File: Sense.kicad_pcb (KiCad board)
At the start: 4 copper layers, 15.2 x 10.2 mm, 10 parts, among them J1 Callistated 1, J2 Callistated 2, U1 SPL07, U2 MMC5603NJ, U3 LSM6DSO32

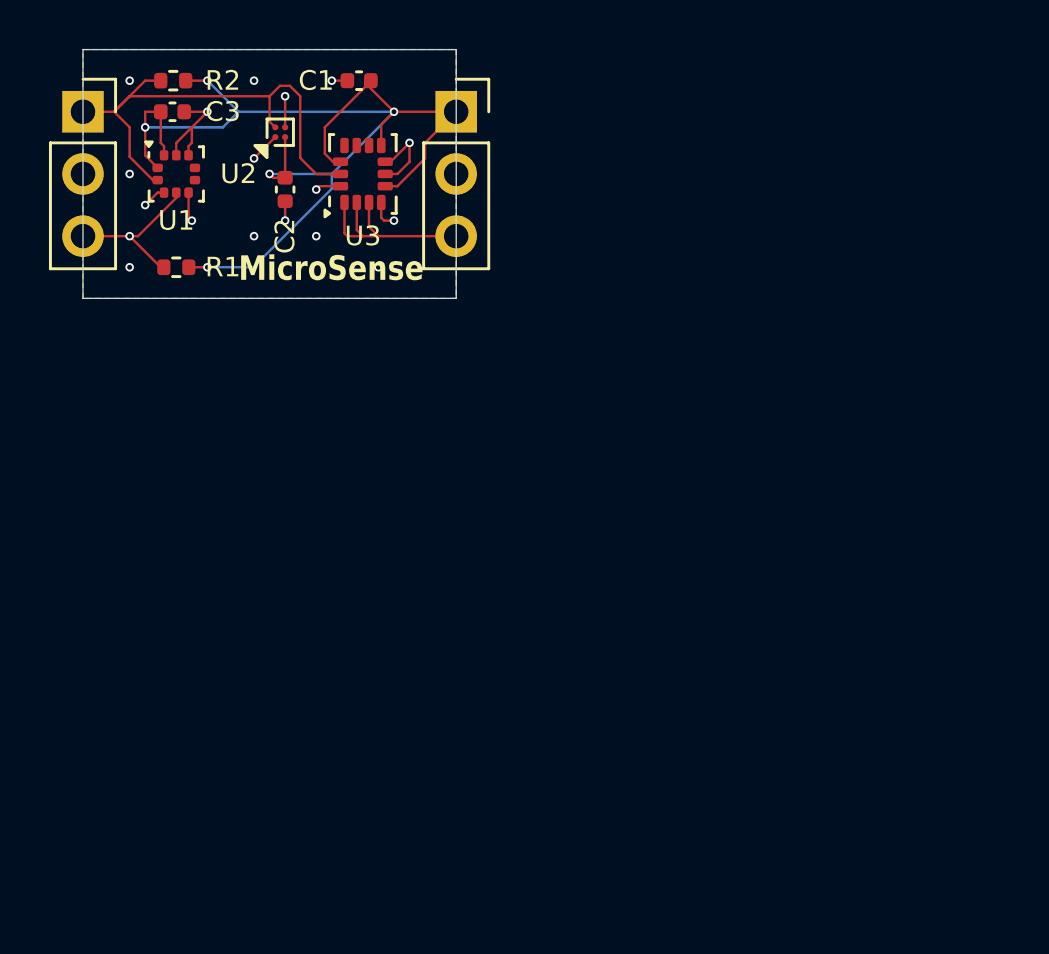
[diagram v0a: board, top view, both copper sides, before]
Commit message: Abandoned castellated pads, updated with LCSC parts
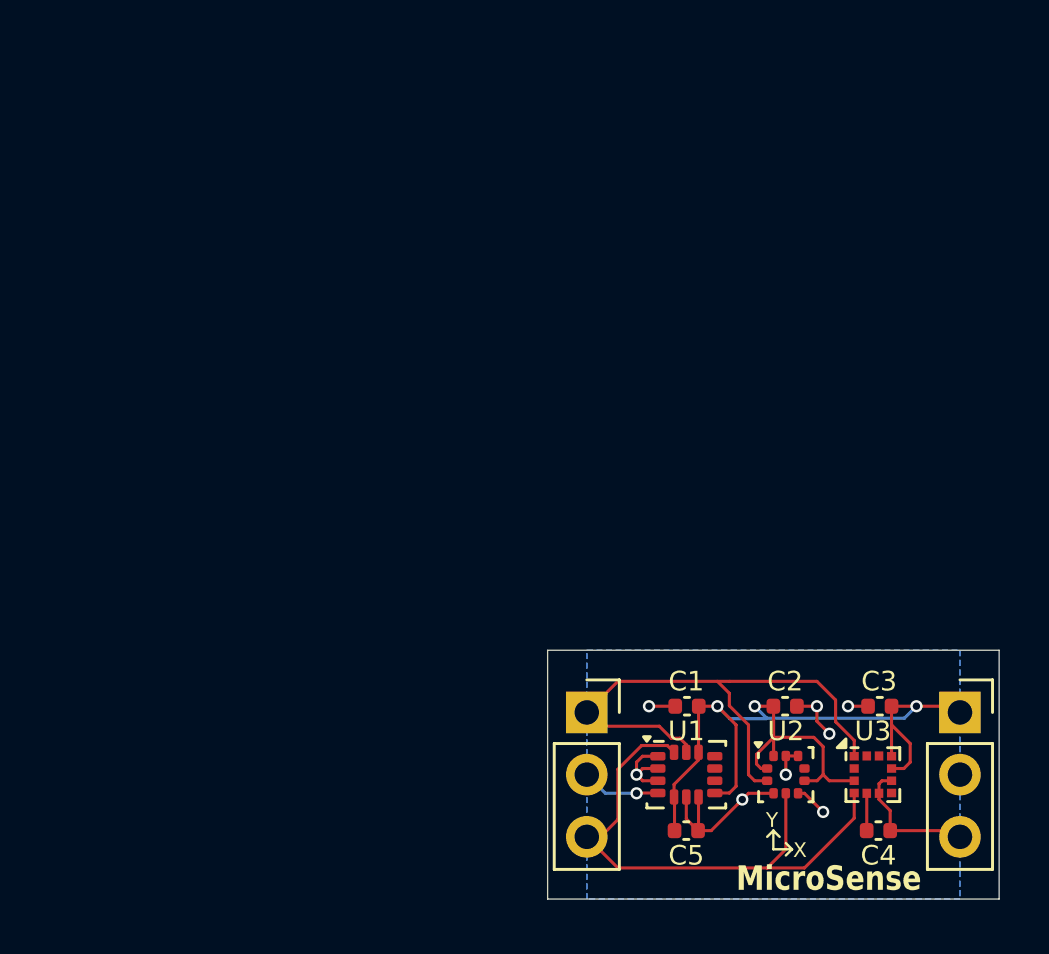
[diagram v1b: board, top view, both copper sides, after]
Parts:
- removed R1, R2: 4K7, Resistor_SMD:R_0402_1005Metric
- removed the U1 at (118.1, 77.5)
- added C4: 220n, Capacitor_SMD:C_0402_1005Metric, F.Cu at (146.8, 104.3)
- added C5: 10u, Capacitor_SMD:C_0402_1005Metric, F.Cu at (138.9, 104.3)
- added U3: LIS2MDL, Package_LGA:LGA-12_2x2mm_P0.5mm, F.Cu at (146.6, 102.0)
- C2: value 2.2u -> 100n
- U2: value MMC5603NJ -> LPS22HB; footprint Package_BGA:WLP-4_0.86x0.86mm_P0.4mm -> Package_LGA:ST_HLGA-10_2x2mm_P0.5mm_LayoutBorder3x2y
- moved C3 37.7 mm to (146.8, 99.2), turned to 180 degrees
- moved U2 33.4 mm to (143.0, 102.0), turned to 0 degrees
- moved J2 32.0 mm to (150.1, 99.5)
- moved J1 32.0 mm to (134.9, 99.5)
- moved C2 29.4 mm to (143.0, 99.2), turned to 0 degrees
- moved C1 28.8 mm to (139.0, 99.2)
- moved U1 27.9 mm to (138.9, 102.0), turned to 0 degrees
- renumbered U3 to U1
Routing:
- net /IMU_INT_1: track 16.1 -> 2.99 mm
- net +3V3: track 48.3 -> 37.4 mm, vias 5 -> 3
- net /SCL: track 20.8 -> 23.3 mm
- net Net-(U3-C1): track 0.00 -> 1.53 mm
- net GND: track 20.9 -> 22.2 mm, vias 14 -> 8
- net /SDA: track 22.6 -> 22.3 mm, vias 3 -> 0
- removed copper zone on In1.Cu, net GND
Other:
- board size 15.2 x 10.2 mm -> 18.4 x 10.2 mm
- copper layers 4 -> 2
- board text added: "X"
- board text added: "Y"

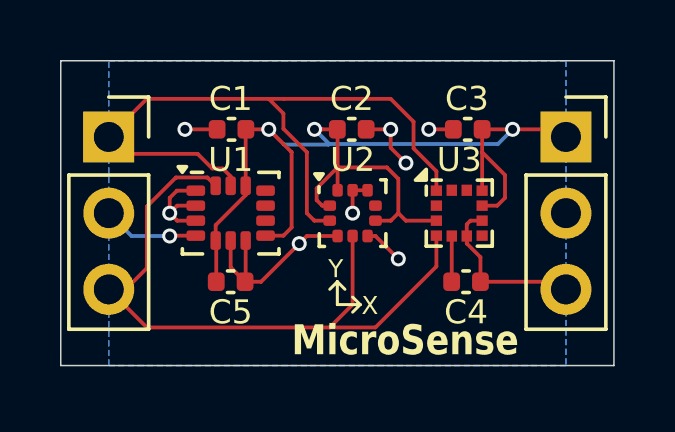
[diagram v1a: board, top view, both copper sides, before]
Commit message: Version C.0
Added high g accelerometer option
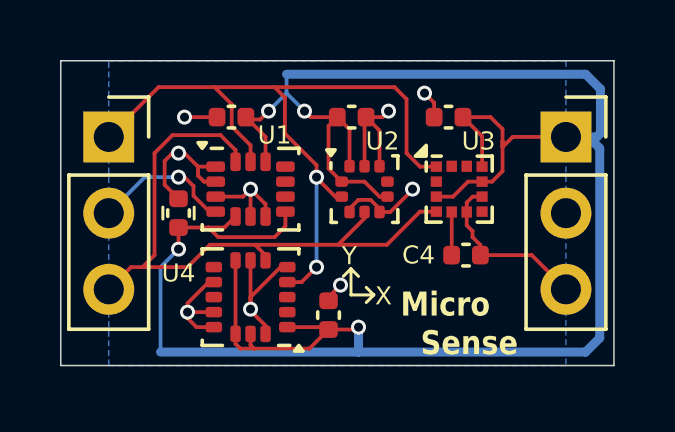
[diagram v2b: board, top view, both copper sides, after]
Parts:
- added C6: 100n, Capacitor_SMD:C_0402_1005Metric, F.Cu at (142.2, 105.4)
- added U4: H3LIS100DLTR, Package_LGA:LGA-16_3x3mm_P0.5mm_LayoutBorder3x5y, F.Cu at (139.6, 104.8)
- U1: value LSM6DSO32 -> LSM6DS3TR-C
- moved C5 2.87 mm to (137.2, 102.0), turned to 90 degrees
- moved U1 1.04 mm to (139.6, 101.2)
- moved U2 0.89 mm to (143.4, 101.2)
- moved C4 0.89 mm to (146.8, 103.4)
- moved U3 0.80 mm to (146.6, 101.2)
- moved C3 0.76 mm to (146.2, 98.8)
- moved C1 0.41 mm to (139.0, 98.8)
- moved C2 0.41 mm to (143.0, 98.8)
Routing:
- net +3V3: track 37.4 -> 77.6 mm, vias 3 -> 4
- net GND: track 22.2 -> 31.8 mm, vias 8 -> 9
- net /SCL: track 23.3 -> 25.6 mm, vias 0 -> 2
- net /IMU_INT_1: track 2.99 -> 4.72 mm
- net /SDA: track 22.3 -> 21.6 mm
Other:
- board text added: "JLCJLCJLC"
- board text added: "Micro Sense"
- board text added: "UCA/T Tutorials 24"
- board text removed: "MicroSense"

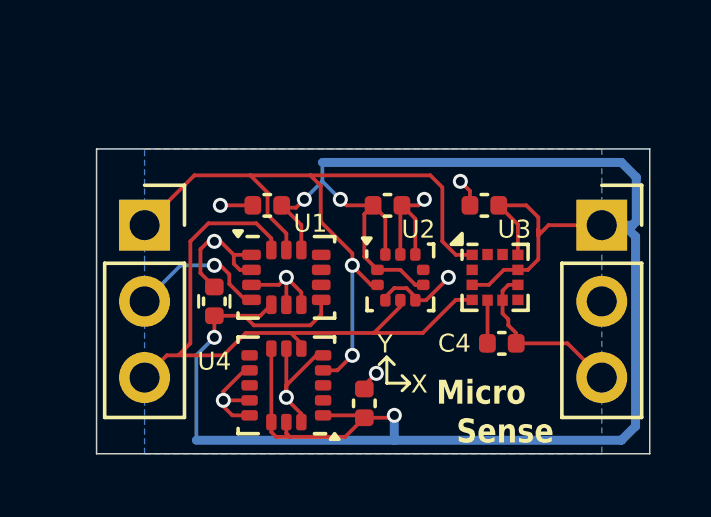
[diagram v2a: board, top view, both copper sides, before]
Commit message: Aligned to grid and fixed pin numbering
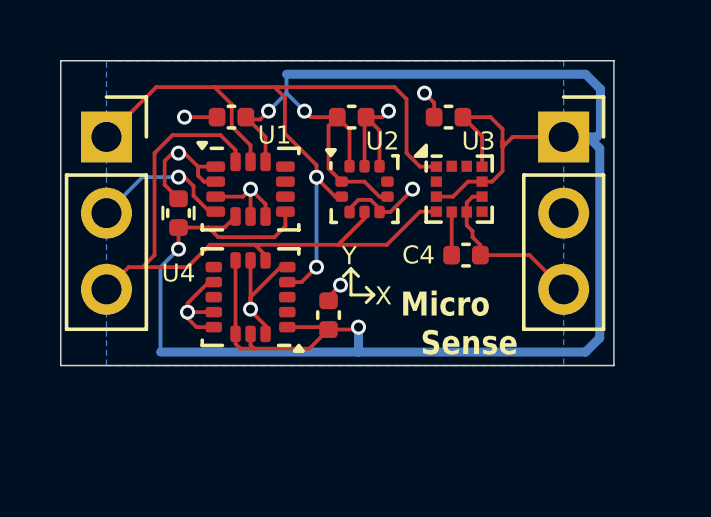
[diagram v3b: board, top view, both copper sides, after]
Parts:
- moved J2 3.20 mm to (148.8, 96.5)
- moved J1 3.20 mm to (133.6, 96.5)
- moved C2 3.17 mm to (141.8, 95.9)
- moved C4 3.17 mm to (145.6, 100.5)
- moved U2 3.17 mm to (142.2, 98.3)
- moved U3 3.17 mm to (145.4, 98.3)
- moved C1 3.17 mm to (137.8, 95.9)
- moved C3 3.17 mm to (145.0, 95.9)
- moved C5 3.17 mm to (136.0, 99.1)
- moved C6 3.17 mm to (141.0, 102.5)
- moved U1 3.17 mm to (138.4, 98.3)
- moved U4 3.17 mm to (138.4, 101.9)
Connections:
- U4 pad 2: (no net) -> unconnected-(U4-NC-Pad2)
- U4 pad 3: (no net) -> unconnected-(U4-NC-Pad3)
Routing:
- net +3V3: track 77.6 -> 76.0 mm

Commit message: Updated after review
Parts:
- moved C2 0.39 mm to (142.1, 96.1)
- moved U2 0.39 mm to (142.5, 98.5)
- moved C1 0.39 mm to (138.1, 96.1)
- moved C3 0.39 mm to (145.3, 96.1)
- moved U4 0.39 mm to (138.7, 102.1)
- moved C4 0.39 mm to (145.9, 100.7)
- moved C5 0.39 mm to (136.3, 99.3)
- moved C6 0.39 mm to (141.3, 102.7)
- moved J1 0.39 mm to (133.9, 96.7)
- moved J2 0.39 mm to (149.2, 96.7)
- moved U1 0.39 mm to (138.7, 98.5)
- moved U3 0.39 mm to (145.7, 98.5)
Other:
- board size 18.4 x 10.2 mm -> 18.2 x 10 mm

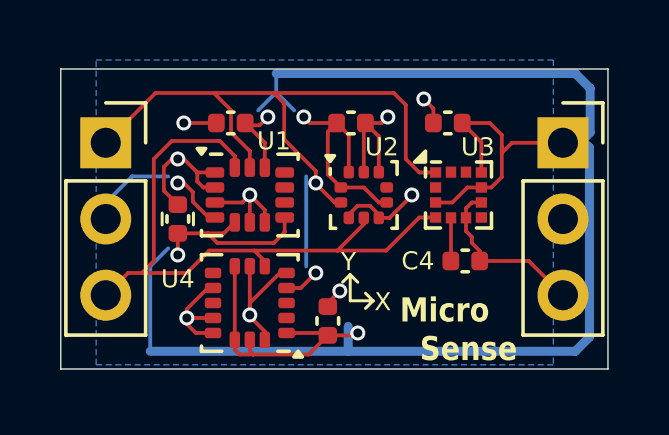
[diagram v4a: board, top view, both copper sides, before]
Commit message: Fixed the couple of things that I broke, updated STEP
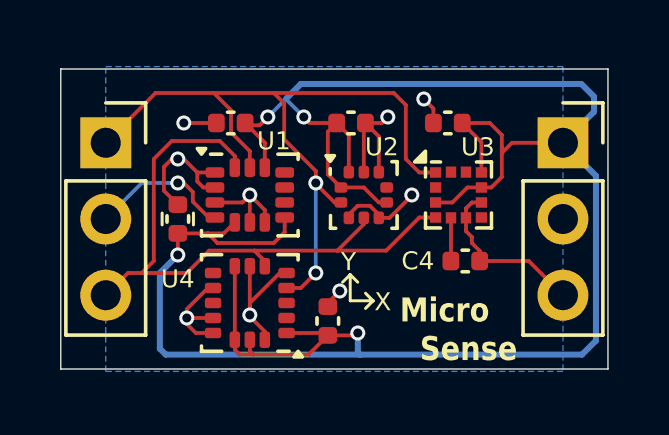
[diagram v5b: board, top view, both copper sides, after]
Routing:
- net +3V3: track 76.0 -> 75.2 mm
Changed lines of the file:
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@@
 	)
 	(footprint "Connector_PinSocket_2.54mm:PinSocket_1x03_P2.54mm_Vertical"
+		(locked yes)
 		(layer "F.Cu")
 		(at 133.924 96.74)
@@
 	)
 	(footprint "Connector_PinSocket_2.54mm:PinSocket_1x03_P2.54mm_Vertical"
+		(locked yes)
 		(layer "F.Cu")
 		(at 149.164 96.74)
@@
 	)
 	(gr_line
-		(start 135.18 100.245)
-		(end 147.945 100.24)
+		(start 135.5 100.465)
+		(end 148.265 100.46)
 		(stroke
 			(width 0.12)
@@
 	)
 	(gr_rect
-		(start 135.18 95.84)
-		(end 147.945 102.14)
+		(start 135.5 96.06)
+		(end 148.265 102.36)
 		(stroke
 			(width 0.12)
@@
 	)
 	(gr_line
-		(start 144.07 102.145)
-		(end 144.07 98.345)
+		(start 144.39 102.365)
+		(end 144.39 98.565)
 		(stroke
 			(width 0.12)
@@
 	)
 	(gr_line
-		(start 135.18 98.34)
-		(end 147.945 98.34)
+		(start 135.5 98.56)
+		(end 148.265 98.56)
 		(stroke
 			(width 0.12)
@@
 		(start 132.424 94.28)
 		(end 150.664 104.28)
+		(locked yes)
 		(stroke
 			(width 0.05)
@@
 	)
 	(gr_text "${TITLE}"
-		(at 147.545 97.74 0)
+		(at 147.865 97.96 0)
 		(layer "B.SilkS")
 		(effects
@@
 	)
 	(gr_text "Date"
-		(at 147.545 101.84 0)
+		(at 147.865 102.06 0)
 		(layer "B.SilkS")
 		(effects
@@
 	)
 	(gr_text "${CURRENT_DATE}"
-		(at 143.435 101.64 0)
+		(at 143.755 101.86 0)
 		(layer "B.SilkS")
 		(effects
@@
 	)
 	(gr_text "${REVISION}"
-		(at 139.245 99.94 0)
+		(at 139.565 100.16 0)
 		(layer "B.SilkS")
 		(effects
@@
 	)
 	(gr_text "JLCJLCJLC"
-		(at 149.164 95.41 -0)
+		(at 149.484 95.63 -0)
 		(layer "B.SilkS")
 		(effects
@@
 	)
 	(gr_text "Rev"
-		(at 147.545 99.94 0)
+		(at 147.865 100.16 0)
 		(layer "B.SilkS")
 		(effects
@@
 	)
 	(gr_text "UCA/T Tutorials 24"
-		(at 144.606 103.85949 -0)
+		(at 144.926 104 -0)
 		(layer "B.SilkS")
 		(effects
@@
 	)
 	(segment
-		(start 135.406 100.85949)
-		(end 135.406 103.69)
-		(width 0.127)
+		(start 149.8 103.8)
+		(end 142.4 103.8)
+		(width 0.2)
 		(layer "B.Cu")
 		(net 1)
 	)
 	(segment
-		(start 139.606 95.05949)
-		(end 139.606 94.43)
-		(width 0.127)
+		(start 136.326 100.47949)
+		(end 135.726 101.07949)
+		(width 0.2)
 		(layer "B.Cu")
 		(net 1)
 	)
 	(segment
-		(start 142.006 103.69)
-		(end 149.57549 103.69)
-		(width 0.3)
+		(start 142.326 103.07949)
+		(end 142.326 103.726)
+		(width 0.2)
 		(layer "B.Cu")
 		(net 1)
 	)
 	(segment
-		(start 149.57549 103.69)
-		(end 150.047 103.21849)
-		(width 0.3)
+		(start 135.926 103.8)
+		(end 135.726 103.6)
+		(width 0.2)
 		(layer "B.Cu")
 		(net 1)
 	)
 	(segment
-		(start 149.94549 96.52)
-		(end 150.07 96.39549)
-		(width 0.3)
+		(start 150.2 95.2)
+		(end 149.77949 94.77949)
+		(width 0.2)
 		(layer "B.Cu")
 		(net 1)
 	)
 	(segment
-		(start 149.66651 96.52)
-		(end 149.94549 96.52)
-		(width 0.3)
+		(start 142.326 103.726)
+		(end 142.4 103.8)
+		(width 0.2)
 		(layer "B.Cu")
 		(net 1)
 	)
 	(segment
-		(start 150.07 96.39549)
-		(end 150.07 94.92349)
-		(width 0.3)
+		(start 150.264 103.336)
+		(end 149.8 103.8)
+		(width 0.2)
 		(layer "B.Cu")
 		(net 1)
 	)
 	(segment
-		(start 140.206 95.65949)
-		(end 139.606 95.05949)
+		(start 140.526 95.87949)
+		(end 139.926 95.27949)
 		(width 0.127)
 		(layer "B.Cu")
@@
 	)
 	(segment
-		(start 136.006 100.25949)
-		(end 135.406 100.85949)
-		(width 0.127)
+		(start 135.726 101.07949)
+		(end 135.726 103.6)
+		(width 0.2)
+		(layer "B.Cu")
+		(net 1)
+	)
+	(segment
+		(start 149.164 96.74)
+		(end 150.2 95.704)
+		(width 0.2)
 		(layer "B.Cu")
 		(net 1)
 	)
 	(segment
-		(start 139.006 95.65949)
-		(end 139.606 95.05949)
+		(start 139.326 95.87949)
+		(end 139.926 95.27949)
 		(width 0.127)
 		(layer "B.Cu")
@@
 	)
 	(segment
-		(start 149.57651 94.43)
-		(end 139.606 94.43)
-		(width 0.3)
+		(start 142.4 103.8)
+		(end 135.926 103.8)
+		(width 0.2)
 		(layer "B.Cu")
 		(net 1)
 	)
 	(segment
-		(start 150.047 103.21849)
-		(end 150.047 96.90049)
-		(width 0.3)
+		(start 140.426 94.77949)
+		(end 139.926 95.27949)
+		(width 0.2)
 		(layer "B.Cu")
 		(net 1)
 	)
 	(segment
-		(start 142.006 103.69)
-		(end 142.006 102.85949)
-		(width 0.3)
+		(start 149.77949 94.77949)
+		(end 140.426 94.77949)
+		(width 0.2)
 		(layer "B.Cu")
 		(net 1)
 	)
 	(segment
-		(start 150.07 94.92349)
-		(end 149.57651 94.43)
-		(width 0.3)
+		(start 150.264 97.84)
+		(end 150.264 103.336)
+		(width 0.2)
 		(layer "B.Cu")
 		(net 1)
 	)
 	(segment
-		(start 150.047 96.90049)
-		(end 149.66651 96.52)
-		(width 0.3)
+		(start 149.164 96.74)
+		(end 150.264 97.84)
+		(width 0.2)
 		(layer "B.Cu")
 		(net 1)
 	)
 	(segment
-		(start 142.006 103.69)
-		(end 135.406 103.69)
-		(width 0.3)
+		(start 150.2 95.704)
+		(end 150.2 95.2)
+		(width 0.2)
 		(layer "B.Cu")
 		(net 1)
@@
 	)
 	(segment
-		(start 140.606 100.85949)
-		(end 140.606 97.85949)
+		(start 140.926 101.07949)
+		(end 140.926 98.07949)
 		(width 0.127)
 		(layer "B.Cu")
@@
 	)
 	(segment
-		(start 134.80451 97.85949)
-		(end 133.604 99.06)
+		(start 135.12451 98.07949)
+		(end 133.924 99.28)
 		(width 0.127)
 		(layer "B.Cu")
@@
 	)
 	(segment
-		(start 136.006 97.85949)
-		(end 134.80451 97.85949)
+		(start 136.326 98.07949)
+		(end 135.12451 98.07949)
 		(width 0.127)
 		(layer "B.Cu")
@@
 		(polygon
 			(pts
-				(xy 133.604 93.98) (xy 148.844 93.98) (xy 148.844 104.14) (xy 133.604 104.14)
+				(xy 133.924 94.2) (xy 149.164 94.2) (xy 149.164 104.36) (xy 133.924 104.36)
 			)
 		)
